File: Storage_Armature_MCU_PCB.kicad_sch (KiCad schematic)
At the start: 121 parts, among them J2 ERROR, J3 User, Q1 20N06, Q2 20N06, U14 USBLC6-2P6, U22 LTV-247, U4 ADP3338AKCZ-3.3RL7, U5 ADP3338AKCZ-3.3RL7

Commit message: VER1.0: добавил BOM и гербера
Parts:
- C1, C105, C106, C107, C108, C109, C110, C111, C112, C113, C12, C13, C14, C15, C2, C20, C21, C26, C30, C34, C35, C44, C45, C47, C48, C49, C65, C66, C68, C69, C70, C71, C73, C74, C8, C9: Description P/N (none) -> Capacitor SMD 50V
- C67: Description P/N (none) -> Polarized capacitor; Product Name (none) -> EEUFR1H331L
- D1: value B2405S-1WR3 -> (none); Description P/N (none) -> DC/DC; Product Name (none) -> B2405S-1WR3
- D10: value SMCJ33A -> (none); Description P/N (none) -> Supressor; Product Name (none) -> SMCJ33A
- D12: value TD301MCANFD -> (none); Description P/N (none) -> CAN Transceiver; Product Name (none) -> TD301MCANFD
- D18: value TD301D485H-A -> (none); Description P/N (none) -> RS485 Transciever; Product Name (none) -> TD301D485H-A
- D20: value BZT52C10 -> (none)
- D21: Description P/N (none) -> ESD Diode
- D9: value WRB2403S-3WR2 -> (none); Description P/N (none) -> DC/DC; Product Name (none) -> WRB2403S-3WR2
- F2: value MF-MSMF050/30X-2 -> (none); Description P/N (none) -> Fuse SMD; Product Name (none) -> MF-MSMF050/30X-2
- F3: value MF-MSMF020 -> (none); Description P/N (none) -> Fuse SMD; Product Name (none) -> MF-MSMF020
- J1: Function (none) -> SWD; Product Name PLS-4 -> KLS1-207-1-04-S; Purpose SWD -> (none)
- J2: value ERROR -> (none); Description P/N (none) -> Connector; Function (none) -> ERROR; Product Name (none) -> DS1073-01-2x3MR2T6
- J3: value User -> (none); footprint Connector_PinSocket_2.54mm:PinSocket_2x08_P2.54mm_Vertical -> Connector_PinHeader_2.54mm:PinHeader_2x08_P2.54mm_Vertical; Description P/N (none) -> Connector; Function (none) -> User; Product Name (none) -> KLS1-207-2-16-S
- J34, J35, J38, J39: Product Name DS1073-01-2x2-MVT6 -> DS1073-01-2x2MR3T6
- J6: Function (none) -> +24V; Product Name DS1073-01-2x2-MVT6 -> DS1073-01-2x2MR3T6; Purpose +24V -> (none)
- JP1, JP2, JP3, JP4, JP5, JP6, JP7: value Jumper_2_Small_Bridged -> (none); Description P/N (none) -> Jumper; Product Name (none) -> DS1027-2ABN0
- L1, L4: Description P/N (none) -> Inductor SMD; Product Name (none) -> ACM2520-301-2P-T002
- L2, L3: Description P/N (none) -> Inductor SMD; Product Name (none) -> LQH32CN6R8M53L
- Q1, Q2: value 20N06 -> (none)
- R1, R2, R37, R39, R40, R47, R48, R49, R54, R55, R57, R58, R6, R78, R87, R88, R89, R90, R91, R92, R93, R94, R95, R96, R97: Description P/N (none) -> Resistor SMD
- TP36, TP37, TP38, TP39, TP40, TP41, TP42, TP43: now left out of the parts list
- U1: Description P/N (none) -> MCU
- U14: value USBLC6-2P6 -> (none); Description P/N (none) -> ESD protection; Product Name (none) -> USBLC6-2P6
- U22: value LTV-247 -> (none); Description P/N (none) -> Photocoupler; Product Name (none) -> LTV-247
- U4, U5: value ADP3338AKCZ-3.3RL7 -> (none); Description P/N (none) -> Linear Regulator; Product Name (none) -> ADP3338AKCZ-3.3RL7
- Y1: value (none) -> 16M
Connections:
- net GND: now also J3.1 (Pin_1), J3.11 (Pin_11), J3.13 (Pin_13), J3.15 (Pin_15), J3.3 (Pin_3), J3.5 (Pin_5), J3.7 (Pin_7), J3.9 (Pin_9); no longer J3.10 (Pin_10), J3.12 (Pin_12), J3.14 (Pin_14), J3.16 (Pin_16), J3.2 (Pin_2), J3.4 (Pin_4), J3.6 (Pin_6), J3.8 (Pin_8)
- net GPIO1: now also J3.2 (Pin_2); no longer J3.1 (Pin_1)
- net GPIO2: now also J3.4 (Pin_4); no longer J3.3 (Pin_3)
- net GPIO3: now also J3.6 (Pin_6); no longer J3.5 (Pin_5)
- net GPIO4: now also J3.8 (Pin_8); no longer J3.7 (Pin_7)
- net GPIO5: now also J3.10 (Pin_10); no longer J3.9 (Pin_9)
- net GPIO6: now also J3.12 (Pin_12); no longer J3.11 (Pin_11)
- net GPIO7: now also J3.14 (Pin_14); no longer J3.13 (Pin_13)
- net GPIO8: now also J3.16 (Pin_16); no longer J3.15 (Pin_15)
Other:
- sheet Solenoid_control_1: file Sch\Solenoid_control.kicad_sch -> Sch/Solenoid_control.kicad_sch
- sheet Solenoid_control_2: file Sch\Solenoid_control.kicad_sch -> Sch/Solenoid_control.kicad_sch
- sheet Solenoid_control_3: file Sch\Solenoid_control.kicad_sch -> Sch/Solenoid_control.kicad_sch
- sheet Solenoid_control_4: file Sch\Solenoid_control.kicad_sch -> Sch/Solenoid_control.kicad_sch

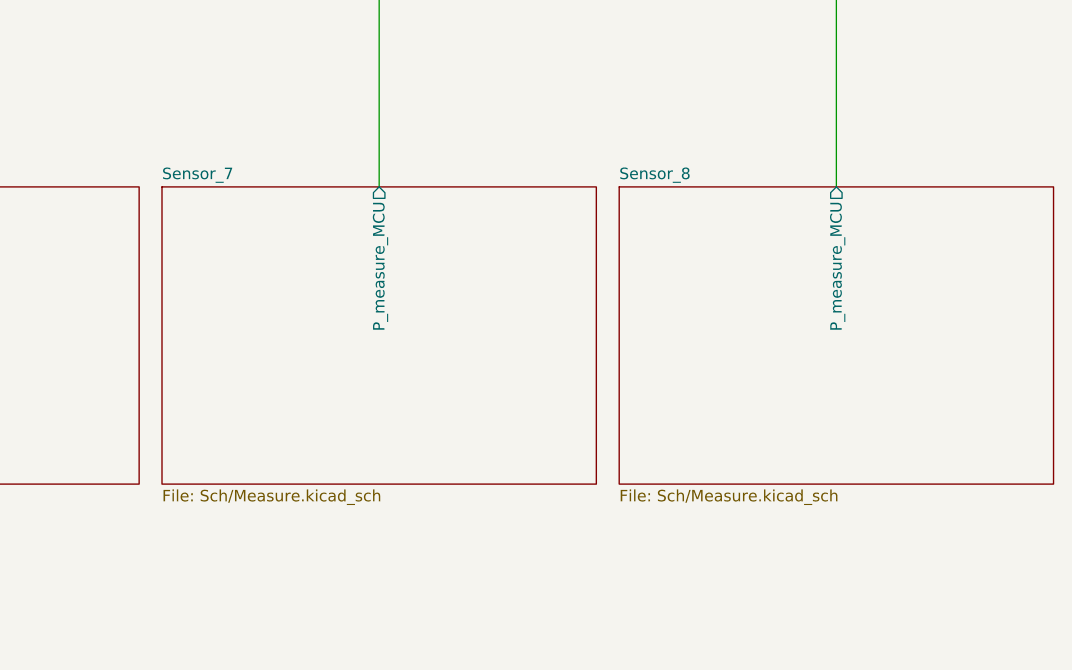
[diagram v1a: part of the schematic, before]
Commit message: VER1.0: исправил каналы расходомеров, добавил папку с отчетным КД
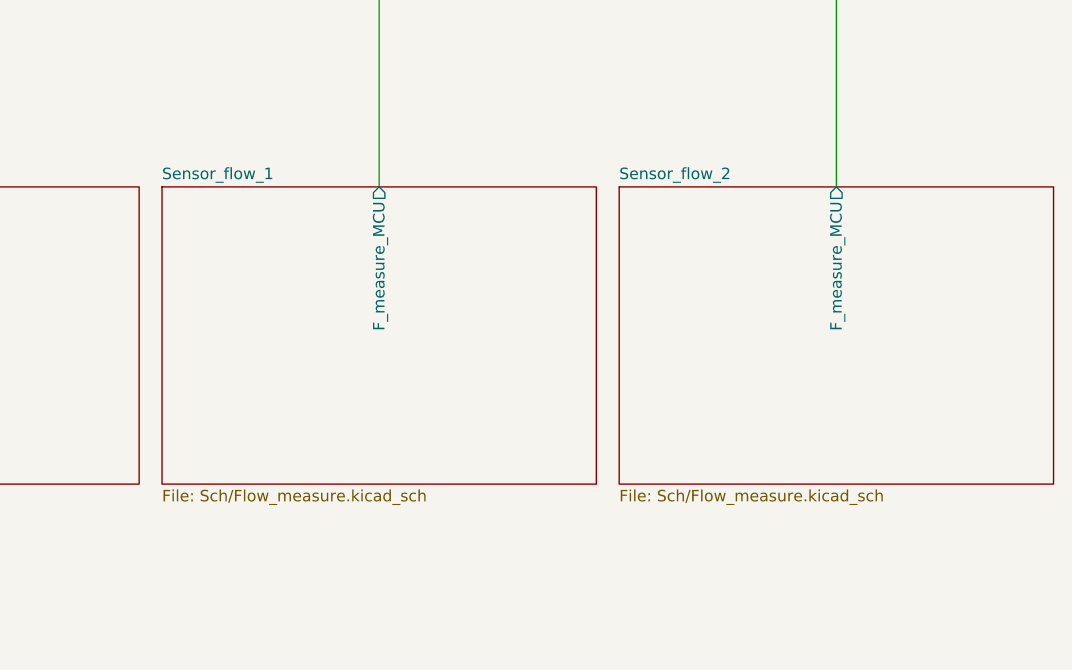
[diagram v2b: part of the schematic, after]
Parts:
- D9: Product Name WRB2403S-3WR2 -> WRB2405S-3WR2
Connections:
- net Sensor_flow_1/P_measure_MCU renamed Sensor_flow_1/F_measure_MCU
- net Sensor_flow_2/P_measure_MCU renamed Sensor_flow_2/F_measure_MCU
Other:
- sheet Sensor_7 renamed Sensor_flow_1
- sheet Sensor_8 renamed Sensor_flow_2
- sheet Sensor_flow_1: file Sch/Measure.kicad_sch -> Sch/Flow_measure.kicad_sch
- sheet Sensor_flow_1 ports: added F_measure_MCU; removed P_measure_MCU
- sheet Sensor_flow_2: file Sch/Measure.kicad_sch -> Sch/Flow_measure.kicad_sch
- sheet Sensor_flow_2 ports: added F_measure_MCU; removed P_measure_MCU
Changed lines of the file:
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@@
 			)
 		)
-		(property "Product Name" "WRB2403S-3WR2"
+		(property "Product Name" "WRB2405S-3WR2"
 			(at 118.11 245.11 0)
 			(hide yes)
@@
 			)
 		)
+		(property "Replacement" ""
+			(at 118.11 245.11 0)
+			(hide yes)
+			(show_name no)
+			(do_not_autoplace no)
+			(effects
+				(font
+					(size 1.27 1.27)
+				)
+			)
+		)
+		(property "Function" ""
+			(at 118.11 245.11 0)
+			(hide yes)
+			(show_name no)
+			(do_not_autoplace no)
+			(effects
+				(font
+					(size 1.27 1.27)
+				)
+			)
+		)
 		(pin "2"
 		)
@@
 			(color 0 0 0 0)
 		)
-		(property "Sheetname" "Sensor_8"
+		(property "Sheetname" "Sensor_flow_2"
 			(at 742.95 474.2684 0)
 			(show_name no)
@@
 			)
 		)
-		(property "Sheetfile" "Sch/Measure.kicad_sch"
+		(property "Sheetfile" "Sch/Flow_measure.kicad_sch"
 			(at 742.95 508.5846 0)
 			(show_name no)
@@
 			)
 		)
-		(pin "P_measure_MCU" output
+		(pin "F_measure_MCU" output
 			(at 767.08 474.98 90)
 			(effects
@@
 			(color 0 0 0 0)
 		)
-		(property "Sheetname" "Sensor_7"
+		(property "Sheetname" "Sensor_flow_1"
 			(at 692.15 474.2684 0)
 			(show_name no)
@@
 			)
 		)
-		(property "Sheetfile" "Sch/Measure.kicad_sch"
+		(property "Sheetfile" "Sch/Flow_measure.kicad_sch"
 			(at 692.15 508.5846 0)
 			(show_name no)
@@
 			)
 		)
-		(pin "P_measure_MCU" output
+		(pin "F_measure_MCU" output
 			(at 716.28 474.98 90)
 			(effects
